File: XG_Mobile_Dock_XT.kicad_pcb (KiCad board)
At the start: 8 copper layers, 220.1 x 93 mm, 229 parts, among them IC1 PI2EQX22024XEAEX, J1 5-1775443-8, J10 SWD, J11 UART, J12 I2C1, J13 39301240, J14 I2C1, J2 20455-040E-76, J3 20455-040E-76, J5 USB_C_Receptacle, J6 455860005, J7 10147430-113T0LF, Q16 AO3401A, Q17 2N7002W, SW1 SW_Push, U1 DS320PR810NJXR, U12 STM32F030C8Tx, U2 DS320PR810NJXR

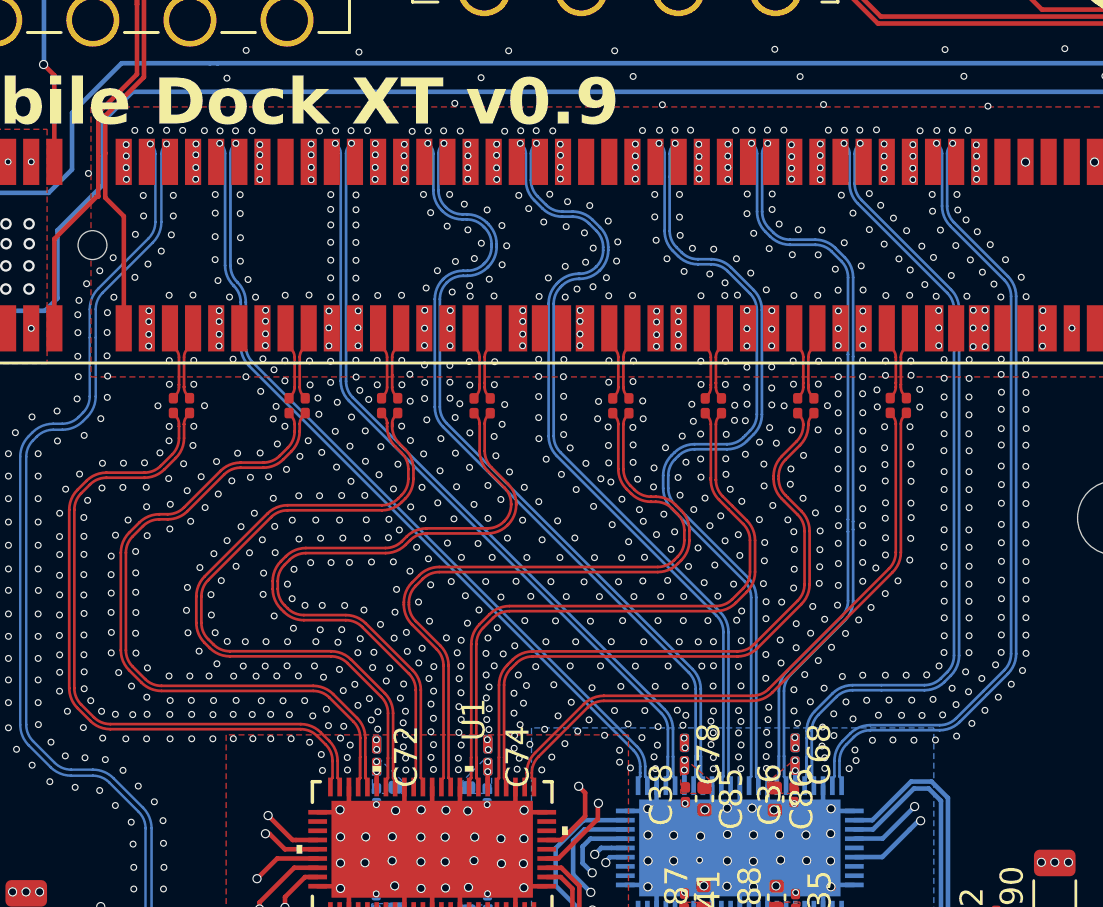
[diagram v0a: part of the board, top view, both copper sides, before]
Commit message: better impedance
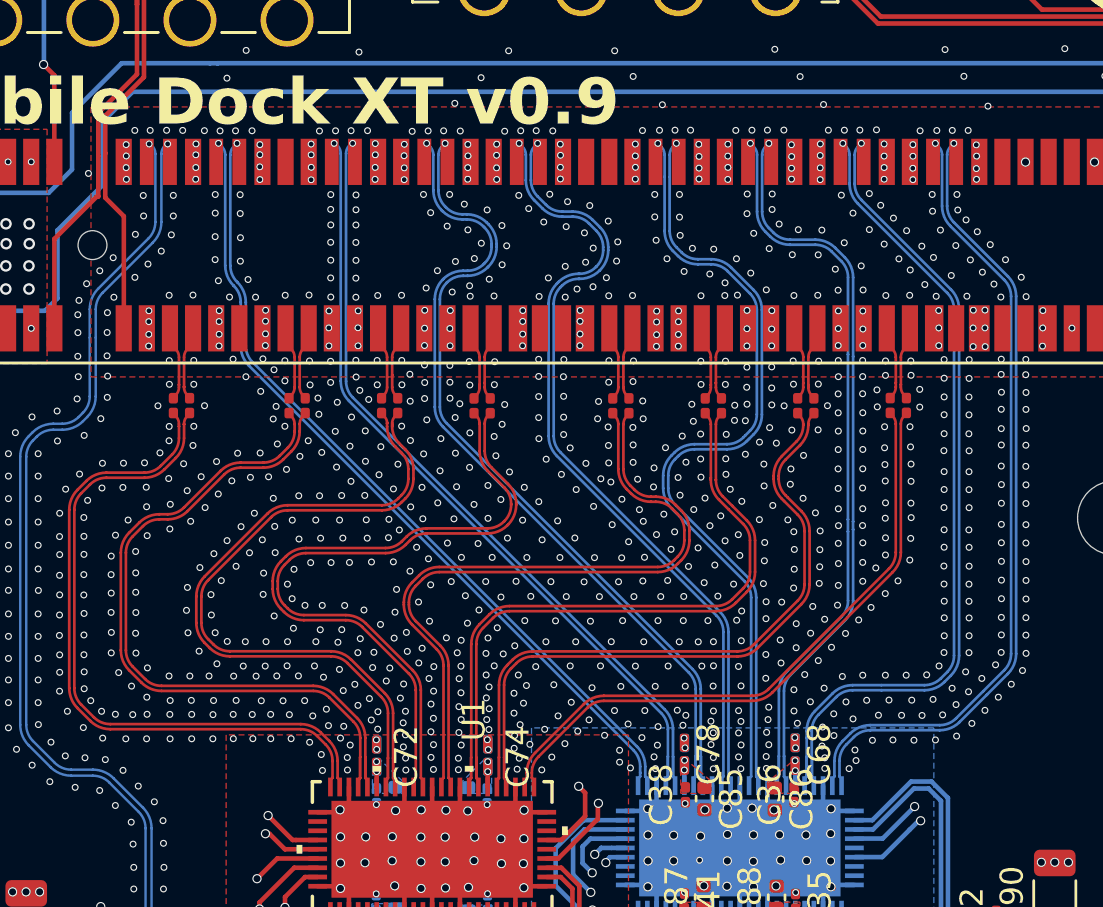
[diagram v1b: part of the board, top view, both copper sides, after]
